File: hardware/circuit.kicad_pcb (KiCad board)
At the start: 2 copper layers, 0 parts

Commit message: feat: first bit of routing and double leds + fixes
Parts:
- added C1: 22uF, Capacitor_SMD:C_0805_2012Metric, F.Cu at (90.5, 113.2)
- added C10: 100nF, Capacitor_SMD:C_0402_1005Metric, F.Cu at (91.8, 95.8)
- added C11: 100nF, Capacitor_SMD:C_0402_1005Metric, F.Cu at (118.8, 104.5)
- added C12: 100nF, Capacitor_SMD:C_0402_1005Metric, F.Cu at (100.0, 91.8)
- added C13: 10uF, Capacitor_SMD:C_0603_1608Metric, F.Cu at (108.8, 111.5)
- added C14: 100nF, Capacitor_SMD:C_0402_1005Metric, F.Cu at (88.3, 82.0)
- added C15: 100nF, Capacitor_SMD:C_0402_1005Metric, F.Cu at (93.5, 82.0)
- added C16: 100nF, Capacitor_SMD:C_0402_1005Metric, F.Cu at (92.3, 77.7)
- added C17: 100nF, Capacitor_SMD:C_0402_1005Metric, B.Cu at (86.5, 77.7)
- added C2: 100nF, Capacitor_SMD:C_0402_1005Metric, F.Cu at (90.5, 116.2)
- added C3: 100nF, Capacitor_SMD:C_0402_1005Metric, F.Cu at (106.8, 78.8)
- added C4: 22uF, Capacitor_SMD:C_0805_2012Metric, F.Cu at (105.2, 88.8)
- added C5: 22uF, Capacitor_SMD:C_0805_2012Metric, F.Cu at (105.2, 85.7)
- added C6: 10uF, Capacitor_SMD:C_0603_1608Metric, F.Cu at (93.5, 92.8)
- added C7: 100nF, Capacitor_SMD:C_0402_1005Metric, F.Cu at (114.2, 97.2)
- added C8: 100nF, Capacitor_SMD:C_0402_1005Metric, F.Cu at (113.8, 105.8)
- added C9: 100nF, Capacitor_SMD:C_0402_1005Metric, F.Cu at (116.8, 106.0)
- added D2: SMAJ15CA, Diode_SMD:D_SMA, F.Cu at (90.8, 109.8)
- added D3: PESD5V0V1BB, Diode_SMD:D_SOD-523, F.Cu at (88.7, 66.9)
- added D4: PESD5V0V1BB, Diode_SMD:D_SOD-523, F.Cu at (86.2, 66.9)
- added J1: VBUS input fly-leads, Connector_Wire:SolderWire-0.25sqmm_1x02_P4.2mm_D0.65mm_OD1.7mm, F.Cu at (88.4, 118.5)
- added J2: Orange TinySLED, Connector_Wire:SolderWire-0.25sqmm_1x04_P4.2mm_D0.65mm_OD1.7mm, F.Cu at (118.0, 70.2)
- added J4: AM32 dual ESC, Connector_Wire:SolderWire-0.25sqmm_1x04_P4.2mm_D0.65mm_OD1.7mm, F.Cu at (89.4, 70.5)
- added L1: 4.7uH, Inductor_SMD:L_Wuerth_MAPI-4020, F.Cu at (102.5, 82.0)
- added Q1: AO3402, Library:SOT-23_L2.9-W1.3-P1.90-LS2.4-BR, F.Cu at (125.5, 65.0)
- added R1: 10kΩ, Resistor_SMD:R_0402_1005Metric, F.Cu at (116.0, 86.0)
- added R10: 33kΩ, Resistor_SMD:R_0402_1005Metric, F.Cu at (100.0, 93.2)
- added R11: 10kΩ, Resistor_SMD:R_0402_1005Metric, F.Cu at (118.2, 99.0)
- added R12: 33Ω, Resistor_SMD:R_0402_1005Metric, F.Cu at (84.0, 66.5)
- added R13: 33Ω, Resistor_SMD:R_0402_1005Metric, F.Cu at (82.0, 66.5)
- added R14: 100kΩ, Resistor_SMD:R_0402_1005Metric, F.Cu at (89.5, 80.0)
- added R15: 100kΩ, Resistor_SMD:R_0402_1005Metric, F.Cu at (92.5, 79.0)
- added R16: 100Ω, Resistor_SMD:R_0402_1005Metric, F.Cu at (121.6, 66.4)
- added R17: 100kΩ, Resistor_SMD:R_0402_1005Metric, F.Cu at (121.6, 64.4)
- added R18: 100kΩ, Resistor_SMD:R_0402_1005Metric, F.Cu at (118.8, 88.0)
- added R19: 10kΩ, Resistor_SMD:R_0402_1005Metric, F.Cu at (113.2, 88.0)
- added R20: 10kΩ, Resistor_SMD:R_0402_1005Metric, F.Cu at (108.0, 94.8)
- added R21: 10kΩ, Resistor_SMD:R_0402_1005Metric, F.Cu at (116.0, 88.0)
- added R3: 10kΩ, Resistor_SMD:R_0402_1005Metric, F.Cu at (117.0, 100.8)
- added R4: 10kΩ, Resistor_SMD:R_0402_1005Metric, F.Cu at (105.8, 124.0)
- added R5: 10kΩ, Resistor_SMD:R_0402_1005Metric, F.Cu at (86.8, 98.8)
- added R6: 33Ω, Resistor_SMD:R_0402_1005Metric, F.Cu at (114.8, 100.8)
- added R7: 33Ω, Resistor_SMD:R_0402_1005Metric, F.Cu at (103.5, 124.0)
- added R8: 33Ω, Resistor_SMD:R_0402_1005Metric, F.Cu at (86.5, 91.2)
- added R9: 120kΩ, Resistor_SMD:R_0402_1005Metric, F.Cu at (100.0, 90.5)
- added REF**: MountingHole_3.2mm_M3_ISO7380_Pad, MountingHole:MountingHole_3.2mm_M3_ISO7380_Pad, F.Cu at (77.8, 57.2)
- added REF**: MountingHole_3.2mm_M3_ISO7380_Pad, MountingHole:MountingHole_3.2mm_M3_ISO7380_Pad, F.Cu at (103.8, 103.2)
- added REF**: MountingHole_3.2mm_M3_ISO7380_Pad, MountingHole:MountingHole_3.2mm_M3_ISO7380_Pad, F.Cu at (129.5, 57.5)
- added TP10: TP_VBAT, TestPoint:TestPoint_Pad_D1.0mm, B.Cu at (100.1, 88.0)
- added TP13: TP_SWDIO, TestPoint:TestPoint_Pad_D1.0mm, B.Cu at (84.2, 56.5)
- added TP14: TP_SWDCK, TestPoint:TestPoint_Pad_D1.0mm, B.Cu at (87.2, 56.5)
- added TP15: TP_GND, TestPoint:TestPoint_Pad_D1.0mm, B.Cu at (90.2, 56.5)
- added U1: Seeed XIAO RP2350, Library:XIAO-RP2350-SMD, F.Cu at (103.7, 64.1)
- added U10: SK9822-EC20, Library:LED-SMD_6P-L2.0-W2.0-P0.80-TL, F.Cu at (89.7, 77.8)
- added U11: SN74HC595PWR, Device:TSSOP-16_L5.0-W4.4-P0.65-LS6.4-BL, F.Cu at (114.5, 93.2)
- added U12: SK9822-EC20, Library:LED-SMD_6P-L2.0-W2.0-P0.80-TL, B.Cu at (89.2, 77.8)
- added U2: AP63205WU-7, Library:TSOT-23-6_L2.9-W1.6-P0.95-LS2.8-BL, F.Cu at (107.3, 81.7)
- added U4: LSM6DSV320XTR, Library:LGA-14_L3.0-W2.5-P0.50-TL, F.Cu at (115.8, 103.2)
- added U5: H3LIS331DLTR, Library:LGA-16_L3.0-W3.0-P0.50-BL, F.Cu at (103.8, 121.2)
- added U6: H3LIS331DLTR, Library:LGA-16_L3.0-W3.0-P0.50-BL, F.Cu at (88.2, 94.2)
- added U7: BetaFPV ELRS Lite, Library:BetaFPV_ELRS_Lite, F.Cu at (118.0, 121.0)
- added U8: SN74AHCT1G125, Library:SC-70-5_L2.0-W1.3-P0.65-LS2.1-BL, F.Cu at (93.7, 84.6)
- added U9: SN74AHCT1G125, Library:SC-70-5_L2.0-W1.3-P0.65-LS2.1-BL, F.Cu at (88.5, 84.8)
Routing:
- net VBUS: track 0.00 -> 73.6 mm
- net 3V3: track 0.00 -> 72.6 mm
- net GND: track 0.00 -> 66.1 mm, vias 0 -> 18
- net 5V: track 0.00 -> 16.0 mm
- net Net-(J2-Pin_3): track 0.00 -> 9.57 mm
- net Net-(U2-SW): track 0.00 -> 8.27 mm
- net /VBAT_SNS: track 0.00 -> 6.16 mm, vias 0 -> 1
- net /IMU Array/CS_B: track 0.00 -> 5.87 mm
- net /SPI_MOSI: track 0.00 -> 5.55 mm
- net /IMU Array/CS_C: track 0.00 -> 4.84 mm
- net Net-(Q1-G): track 0.00 -> 4.79 mm
- net /IMU Array/CS_A: track 0.00 -> 3.86 mm
- net /IMU Array/MISO_C: track 0.00 -> 2.20 mm
- net /IMU Array/MISO_A: track 0.00 -> 1.85 mm
- net /SPI_SCK: track 0.00 -> 1.80 mm
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- added copper zone on B.Cu, net GND
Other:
- board outline added: 60 x 73.2 mm

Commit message: feat: pcb routing
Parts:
- renumbered REF** to Mountinghole-1, REF** to Mountinghole-2, REF** to Mountinghole-3
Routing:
- net 3V3: track 72.6 -> 246.7 mm, vias 0 -> 3
- net 5V: track 16.0 -> 163.4 mm, vias 0 -> 5
- net /SPI_MOSI: track 5.55 -> 148.9 mm, vias 0 -> 3
- net /SPI_SCK: track 1.80 -> 110.9 mm, vias 0 -> 4
- net /CRSF_TX: track 0.00 -> 88.4 mm
- net /SEL_LAT: track 0.00 -> 59.1 mm, vias 0 -> 2
- net /CRSF_RX: track 0.00 -> 50.4 mm, vias 0 -> 2
- net GND: track 66.1 -> 113.9 mm, vias 18 -> 28
- net /SEL_OE_N: track 0.00 -> 43.5 mm, vias 0 -> 2
- net /LED_OE_N: track 0.00 -> 42.1 mm, vias 0 -> 4
- net /VBAT_SNS: track 6.16 -> 47.2 mm, vias 1 -> 2
- net /IMU Array/CS_B: track 5.87 -> 46.0 mm
- net /IMU Array/CS_C: track 4.84 -> 41.9 mm, vias 0 -> 2
- net /HEAD_LED: track 0.00 -> 30.0 mm, vias 0 -> 2
- net VBUS: track 73.6 -> 94.9 mm
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
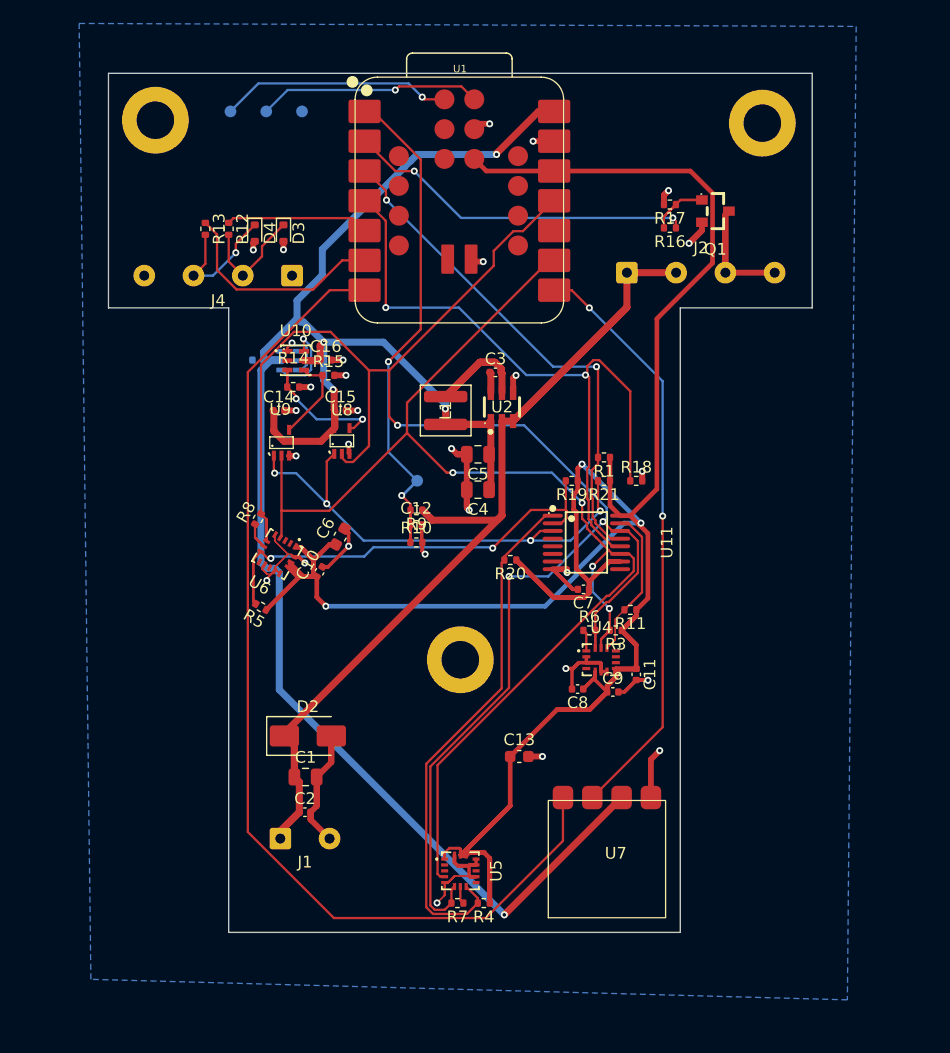
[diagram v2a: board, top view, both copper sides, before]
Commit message: feat: 4 layer route
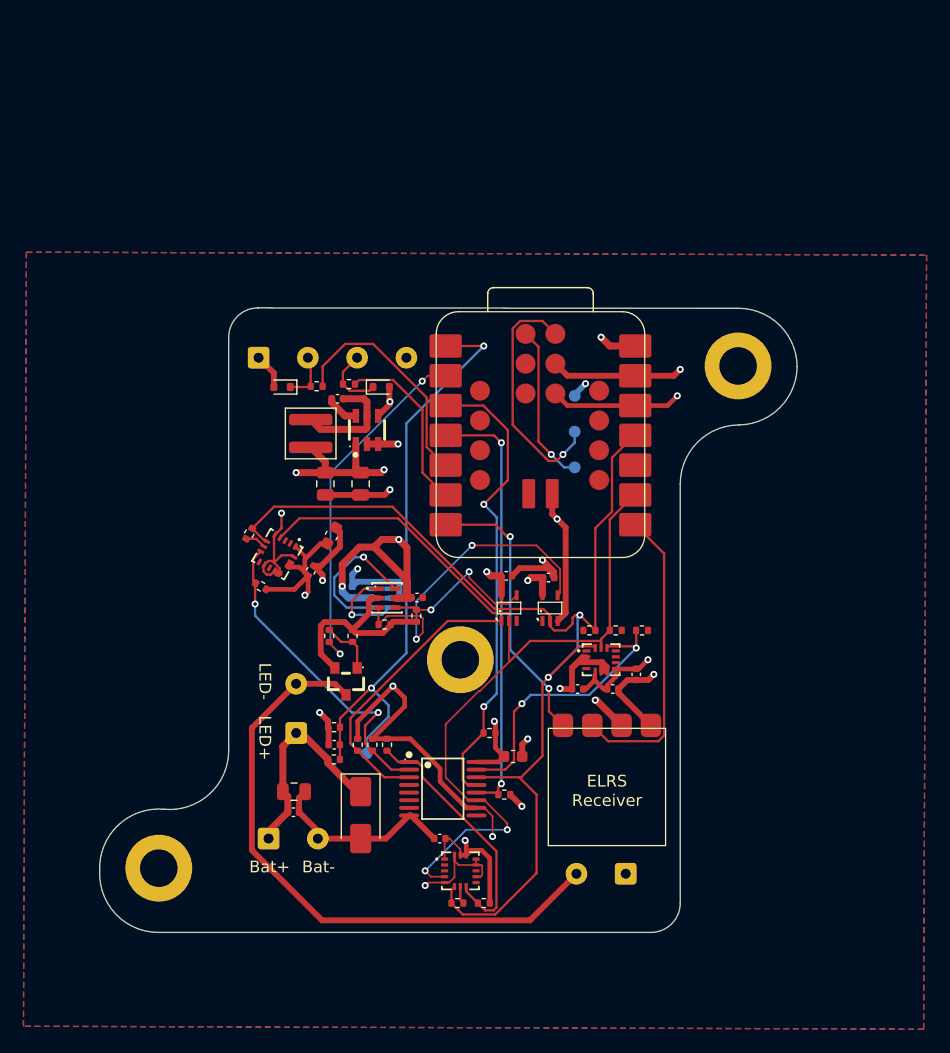
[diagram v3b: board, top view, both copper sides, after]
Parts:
- removed Mountinghole-1: MountingHole_3.2mm_M3_ISO7380_Pad, MountingHole:MountingHole_3.2mm_M3_ISO7380_Pad
- added J3: Orange TinySLED, Connector_Wire:SolderWire-0.25sqmm_1x02_P4.2mm_D0.65mm_OD1.7mm, F.Cu at (117.8, 121.5)
- added MountingHole-2: MountingHole_3.2mm_M3_ISO7380_Pad, MountingHole:MountingHole_3.2mm_M3_ISO7380_Pad, F.Cu at (127.4, 78.2)
- J2: footprint Connector_Wire:SolderWire-0.25sqmm_1x04_P4.2mm_D0.65mm_OD1.7mm -> Connector_Wire:SolderWire-0.25sqmm_1x02_P4.2mm_D0.65mm_OD1.7mm
- moved Mountinghole-2 63.8 mm to (78.0, 121.0)
- moved Q1 51.0 mm to (94.0, 105.1), turned to 90 degrees
- moved J2 48.3 mm to (89.8, 109.5), turned to 90 degrees
- moved R17 45.7 mm to (94.6, 101.2), turned to 90 degrees
- moved R16 45.3 mm to (92.6, 101.2), turned to 90 degrees
- moved TP13 42.2 mm to (113.5, 86.8), turned to 0 degrees
- moved TP14 37.9 mm to (113.5, 83.8), turned to 0 degrees
- moved TP15 33.6 mm to (113.5, 80.8), turned to 0 degrees
- moved R21 30.8 mm to (95.0, 110.5), turned to -90 degrees
- moved R18 29.0 mm to (107.5, 114.8)
- moved R19 28.2 mm to (96.2, 110.5), turned to -90 degrees
- moved R1 25.4 mm to (106.2, 109.5)
- moved C7 24.5 mm to (102.0, 118.5)
- moved U11 24.3 mm to (102.2, 114.2)
- moved C14 24.0 mm to (107.7, 96.1)
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- renumbered U7 to ELRS
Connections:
- J2 pad 2: VBUS -> Net-(J2-Pin_2)
- Q1 pad 3: Net-(J2-Pin_3) -> Net-(J2-Pin_2)
- R15 pad 1: /Status Leds/LED_CK -> GND
- R15 pad 2: GND -> /Status Leds/LED_CK
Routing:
- net 3V3: track 246.7 -> 78.0 mm, vias 3 -> 7
- net 5V: track 163.4 -> 49.1 mm, vias 5 -> 8
- net /CRSF_TX: track 88.4 -> 23.9 mm, vias 0 -> 2
- net Net-(J2-Pin_2): track 0.00 -> 52.2 mm
- net /SPI_MOSI: track 148.9 -> 100.4 mm, vias 3 -> 2
- net VBUS: track 94.9 -> 60.6 mm, vias 0 -> 1
- net /SPI_SCK: track 110.9 -> 81.0 mm, vias 4 -> 2
- net /CRSF_RX: track 50.4 -> 25.9 mm, vias 2 -> 0
- net /IMU Array/CS_B: track 46.0 -> 22.4 mm
- net /SEL_LAT: track 59.1 -> 37.1 mm
- net GND: track 113.9 -> 133.8 mm, vias 28 -> 15
- net /LED_OE_N: track 42.1 -> 24.6 mm, vias 4 -> 0
- net /Status Leds/LED_DI: track 12.0 -> 28.2 mm
- net Net-(J2-Pin_3): track 14.5 -> 0.00 mm
- net /IMU Array/CS_C: track 41.9 -> 27.6 mm
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- added copper zone on In1.Cu, net 3V3
- added copper zone on In1.Cu, net 5V
- added copper zone on F.Cu, net GND
- added copper zone on In2.Cu, net GND
- added copper zone on In1.Cu, net VBUS
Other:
- board size 60 x 73.2 mm -> 59.5 x 53.2 mm
- copper layers 2 -> 4
- board text added: "Bat+"
- board text added: "Bat-"
- board text added: "LED+"
- board text added: "LED-"
- board text added: "Receiver"

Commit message: feat: add stiching vias
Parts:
- moved TP15 0.25 mm to (113.5, 81.0)
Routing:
- net 5V: track 49.1 -> 61.7 mm
- net GND: track 133.8 -> 133.4 mm, vias 15 -> 42
- net VBUS: vias 1 -> 2
- net 3V3: vias 7 -> 8
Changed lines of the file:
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@@
 		(placed yes)
 		(layer "B.Cu")
-		(at 113.5 80.75)
+		(at 113.5 81)
 		(descr "SMD pad as test Point, diameter 1.0mm")
 		(tags "test point SMD pad")
@@
 	)
 	(via
+		(at 122 84)
+		(size 0.6)
+		(drill 0.3)
+		(layers "F.Cu" "B.Cu")
+		(net "3V3")
+	)
+	(via
 		(at 106.65 108.5)
 		(size 0.6)
@@
 	)
 	(via
+		(at 84.75 124.25)
+		(size 0.6)
+		(drill 0.3)
+		(layers "F.Cu" "B.Cu")
+		(net "GND")
+	)
+	(via
+		(at 76.5 117.25)
+		(size 0.6)
+		(drill 0.3)
+		(layers "F.Cu" "B.Cu")
+		(net "GND")
+	)
+	(via
+		(at 97 123.75)
+		(size 0.6)
+		(drill 0.3)
+		(layers "F.Cu" "B.Cu")
+		(net "GND")
+	)
+	(via
 		(at 109.5 110)
 		(size 0.6)
@@
 	)
 	(via
+		(at 92.75 116)
+		(size 0.6)
+		(drill 0.3)
+		(layers "F.Cu" "B.Cu")
+		(net "GND")
+	)
+	(via
 		(at 91.75 107.75)
 		(size 0.6)
@@
 	)
 	(via
+		(at 113.742883 95.863195)
+		(size 0.6)
+		(drill 0.3)
+		(layers "F.Cu" "B.Cu")
+		(net "GND")
+	)
+	(via
 		(at 112.25 105.7)
 		(size 0.6)
@@
 	)
 	(via
-		(at 114.428623 79.713109)
+		(at 111.75 82.75)
+		(size 0.6)
+		(drill 0.3)
+		(layers "F.Cu" "B.Cu")
+		(net "GND")
+	)
+	(via
+		(at 113.5 79.75)
+		(size 0.6)
+		(drill 0.3)
+		(layers "F.Cu" "B.Cu")
+		(net "GND")
+	)
+	(via
+		(at 124.5 81.25)
+		(size 0.6)
+		(drill 0.3)
+		(layers "F.Cu" "B.Cu")
+		(net "GND")
+	)
+	(via
+		(at 114.25 90.5)
 		(size 0.6)
 		(drill 0.3)
@@
 	)
 	(via
+		(at 87.25 86.75)
+		(size 0.6)
+		(drill 0.3)
+		(layers "F.Cu" "B.Cu")
+		(net "GND")
+	)
+	(via
+		(at 83.5 121)
+		(size 0.6)
+		(drill 0.3)
+		(layers "F.Cu" "B.Cu")
+		(net "GND")
+	)
+	(via
+		(at 121.5 89.25)
+		(size 0.6)
+		(drill 0.3)
+		(layers "F.Cu" "B.Cu")
+		(net "GND")
+	)
+	(via
+		(at 119.5 106.25)
+		(size 0.6)
+		(drill 0.3)
+		(layers "F.Cu" "B.Cu")
+		(net "GND")
+	)
+	(via
 		(at 100.75 122.5)
 		(size 0.6)
@@
 	)
 	(via
+		(at 82 124.25)
+		(size 0.6)
+		(drill 0.3)
+		(layers "F.Cu" "B.Cu")
+		(net "GND")
+	)
+	(via
+		(at 114.25 76.75)
+		(size 0.6)
+		(drill 0.3)
+		(layers "F.Cu" "B.Cu")
+		(net "GND")
+	)
+	(via
 		(at 88.5 90.75)
 		(size 0.6)
@@
 	)
 	(via
+		(at 125 74.5)
+		(size 0.6)
+		(drill 0.3)
+		(layers "F.Cu" "B.Cu")
+		(net "GND")
+	)
+	(via
+		(at 122.5 75.25)
+		(size 0.6)
+		(drill 0.3)
+		(layers "F.Cu" "B.Cu")
+		(net "GND")
+	)
+	(via
+		(at 83 117)
+		(size 0.6)
+		(drill 0.3)
+		(layers "F.Cu" "B.Cu")
+		(net "GND")
+	)
+	(via
+		(at 85.5 106.5)
+		(size 0.6)
+		(drill 0.3)
+		(layers "F.Cu" "B.Cu")
+		(net "GND")
+	)
+	(via
+		(at 93.5 122.25)
+		(size 0.6)
+		(drill 0.3)
+		(layers "F.Cu" "B.Cu")
+		(net "GND")
+	)
+	(via
 		(at 109 115.75)
 		(size 0.6)
@@
 	)
 	(via
+		(at 89 74.75)
+		(size 0.6)
+		(drill 0.3)
+		(layers "F.Cu" "B.Cu")
+		(net "GND")
+	)
+	(via
 		(at 97.75 81.25)
 		(size 0.6)
@@
 	)
 	(via
+		(at 94.25 74.75)
+		(size 0.6)
+		(drill 0.3)
+		(layers "F.Cu" "B.Cu")
+		(net "GND")
+	)
+	(via
 		(at 120.25 104.5)
 		(size 0.6)
@@
 		(net "GND")
 	)
+	(via
+		(at 98.75 74.75)
+		(size 0.6)
+		(drill 0.3)
+		(layers "F.Cu" "B.Cu")
+		(net "GND")
+	)
+	(via
+		(at 102.25 97)
+		(size 0.6)
+		(drill 0.3)
+		(layers "F.Cu" "B.Cu")
+		(net "GND")
+	)
+	(via
+		(at 99.25 119)
+		(size 0.6)
+		(drill 0.3)
+		(layers "F.Cu" "B.Cu")
+		(net "GND")
+	)
+	(via
+		(at 80.5 117.25)
+		(size 0.6)
+		(drill 0.3)
+		(layers "F.Cu" "B.Cu")
+		(net "GND")
+	)
+	(via
+		(at 85.5 81.25)
+		(size 0.6)
+		(drill 0.3)
+		(layers "F.Cu" "B.Cu")
+		(net "GND")
+	)
+	(via
+		(at 89 100)
+		(size 0.6)
+		(drill 0.3)
+		(layers "F.Cu" "B.Cu")
+		(net "GND")
+	)
 	(segment
 		(start 98.55 96.6)
@@
 	)
 	(segment
-		(start 113.5 80.641732)
+		(start 113.5 79.75)
 		(end 113.5 80.75)
 		(width 0.5)
@@
 	)
 	(segment
-		(start 114.428623 79.713109)
-		(end 113.5 80.641732)
-		(width 0.5)
-		(layer "B.Cu")
-		(net "GND")
-	)
-	(segment
 		(start 94.54 97.02)
 		(end 94.54 95.96)
@@
 	)
 	(via
+		(at 78.5 125.25)
+		(size 0.6)
+		(drill 0.3)
+		(layers "F.Cu" "B.Cu")
+		(net "VBUS")
+	)
+	(via
 		(at 98.44 84.86)
 		(size 0.6)
@@
 	)
 	(segment
+		(start 109.5 100.95)
+		(end 109.5 96.5)
+		(width 0.6)
+		(layer "In1.Cu")
+		(net "5V")
+	)
+	(segment
+		(start 115.25 106.7)
+		(end 109.5 100.95)
+		(width 0.6)
+		(layer "In1.Cu")
+		(net "5V")
+	)
+	(segment
 		(start 111.272182 86.3)
 		(end 111.95 86.3)
@@
 		(polygon
 			(pts
-				(xy 110 120.75) (xy 110 107) (xy 122.5 107) (xy 122.5 120.75)
+				(xy 110 120.75) (xy 110 109) (xy 122.5 109) (xy 122.5 120.75)
 			)
 		)
@@
 			(pts
 				(xy 112.75 95) (xy 103.878717 95) (xy 102 91.5) (xy 102.75 80.5) (xy 89.25 85.75) (xy 89.25 89.25)
-				(xy 90.5 90.25) (xy 93.75 90.25) (xy 98.25 95) (xy 100.75 97.25) (xy 104.25 98.25) (xy 105 101.75)
-				(xy 110 107.75) (xy 120 107.75) (xy 120 105.75) (xy 112.75 105.75) (xy 112.75 104.25) (xy 112.75 101.75)
+				(xy 90.5 90.25) (xy 93.75 90.25) (xy 98.25 95) (xy 100.75 97.25) (xy 104.25 98.25) (xy 112.75 98.25)
 			)
 		)

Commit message: feat: add more vias
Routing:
- net GND: vias 42 -> 49
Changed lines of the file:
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@@
+	)
+	(via
+		(at 109.25 86.25)
+		(size 0.6)
+		(drill 0.3)
+		(layers "F.Cu" "B.Cu")
+		(net "GND")
 	)
 	(via
@@
 	)
 	(via
+		(at 113.75 74.5)
+		(size 0.6)
+		(drill 0.3)
+		(layers "F.Cu" "B.Cu")
+		(net "GND")
+	)
+	(via
 		(at 87.25 86.75)
 		(size 0.6)
@@
 	)
 	(via
+		(at 110.25 92)
+		(size 0.6)
+		(drill 0.3)
+		(layers "F.Cu" "B.Cu")
+		(net "GND")
+	)
+	(via
 		(at 119.5 106.25)
 		(size 0.6)
@@
 	)
 	(via
+		(at 107 74.5)
+		(size 0.6)
+		(drill 0.3)
+		(layers "F.Cu" "B.Cu")
+		(net "GND")
+	)
+	(via
 		(at 114.25 76.75)
 		(size 0.6)
@@
 	)
 	(via
+		(at 99.75 88.75)
+		(size 0.6)
+		(drill 0.3)
+		(layers "F.Cu" "B.Cu")
+		(net "GND")
+	)
+	(via
 		(at 110.75 94.75)
 		(size 0.6)
@@
 	)
 	(via
+		(at 107.75 90.25)
+		(size 0.6)
+		(drill 0.3)
+		(layers "F.Cu" "B.Cu")
+		(net "GND")
+	)
+	(via
 		(at 95 95.5)
 		(size 0.6)
 		(drill 0.3)
+		(layers "F.Cu" "B.Cu")
+		(net "GND")
+	)
+	(via
+		(at 106.5 78.25)
+		(size 0.6)
+		(drill 0.3)
